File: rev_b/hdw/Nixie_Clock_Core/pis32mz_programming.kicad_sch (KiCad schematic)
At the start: 13 parts, among them J801 PICKIT4, Q801 BSS214NW, SW801 MRST

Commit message: lots of rev B control board schematic progress
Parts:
- renumbered C801 to C?, C802 to C?, D801 to D?, J801 to J?, Q801 to Q?, R805 to R?, R801 to R?, R803 to R?, SW801 to SW?

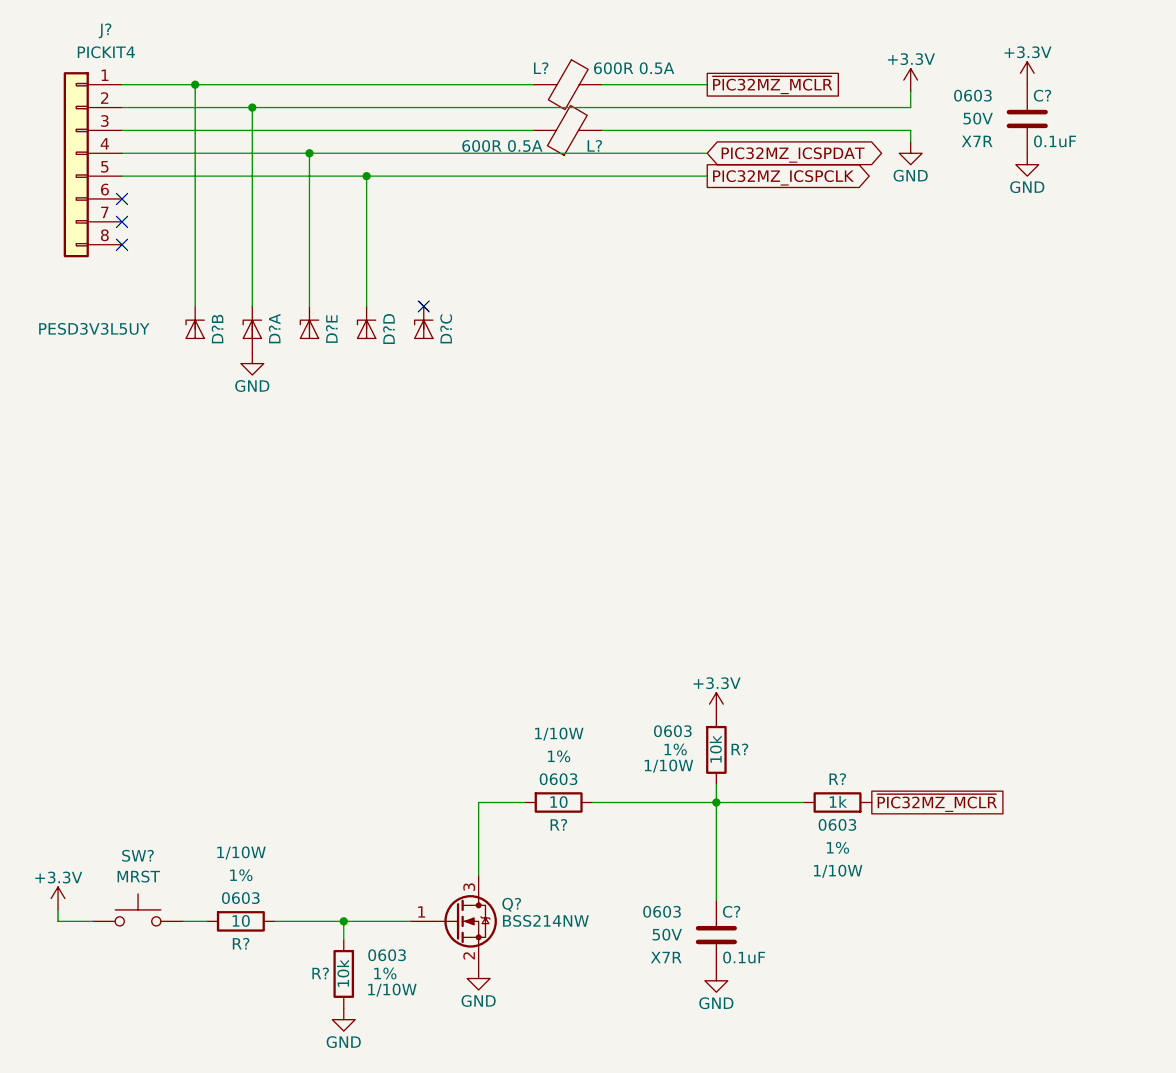
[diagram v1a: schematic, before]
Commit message: updated footprints, ran some DRC
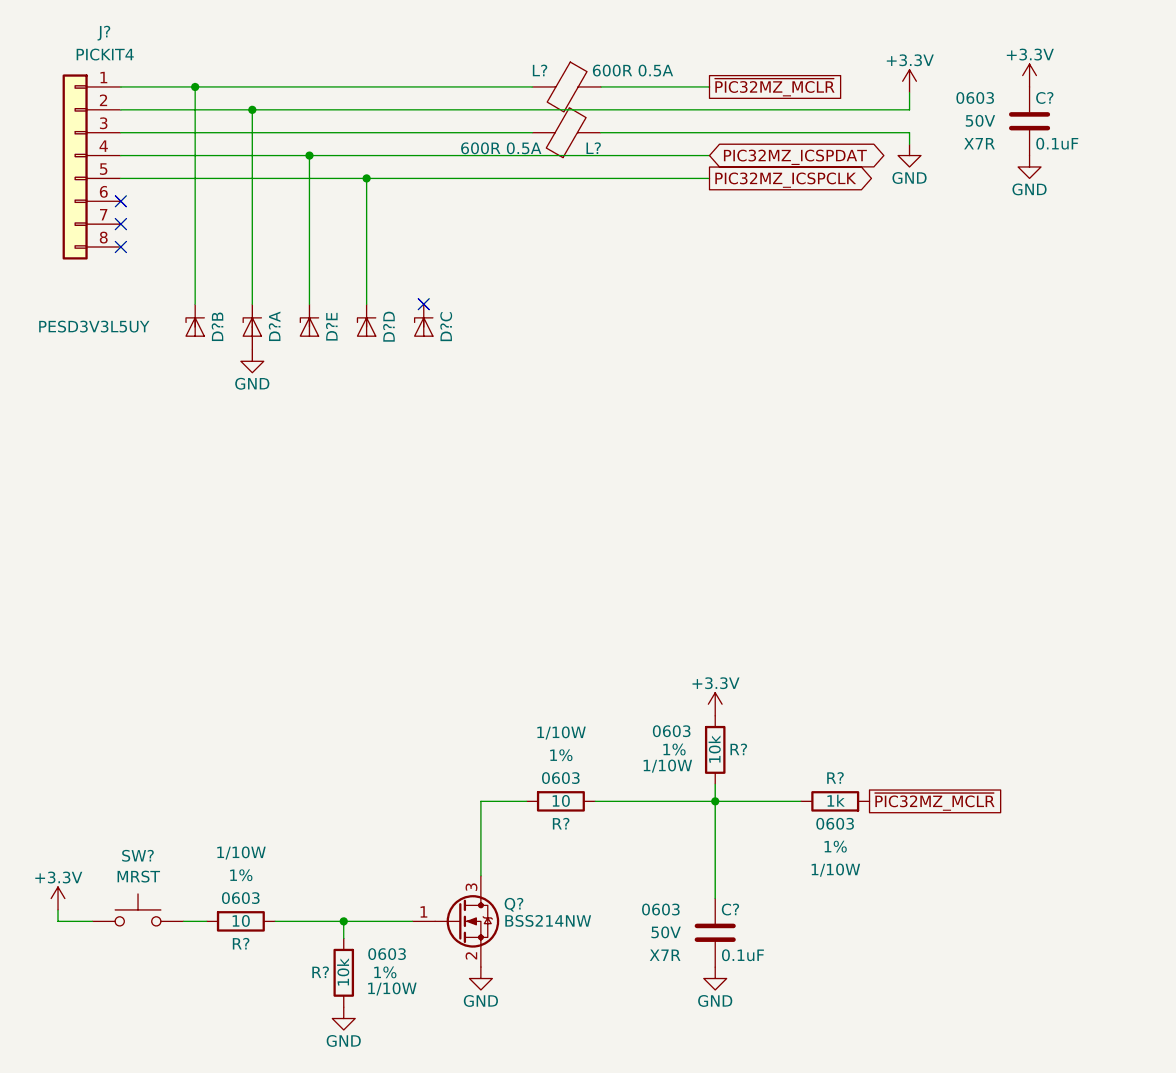
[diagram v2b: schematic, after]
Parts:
- C? (x2): Digi-Key PN 399-7845-1-ND -> (none)
- L? (x2): Digi-Key PN 732-1593-1-ND -> (none)
- R?: Digi-Key PN 311-1.00KHRCT-ND -> (none)
- R? (x4): Digi-Key PN YAG2321CT-ND -> (none)
- SW?: footprint Buttons_Switches_THT:SW_PUSH_6mm -> Button_Switch_THT:SW_PUSH_6mm

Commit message: hid all passive refdes on core PCB
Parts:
- C? (x2): Digi-Key PN (none) -> 1276-1935-1-ND
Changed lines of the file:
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@@
       (effects (font (size 1.27 1.27)) (justify right))
     )
-    (property "Digi-Key PN" "" (at 161.29 130.81 0)
+    (property "Digi-Key PN" "1276-1935-1-ND" (at 161.29 130.81 0)
       (effects (font (size 1.524 1.524)) hide)
     )
@@
       (effects (font (size 1.27 1.27)) (justify right))
     )
-    (property "Digi-Key PN" "" (at 196.215 40.64 0)
+    (property "Digi-Key PN" "1276-1935-1-ND" (at 196.215 40.64 0)
       (effects (font (size 1.524 1.524)) hide)
     )

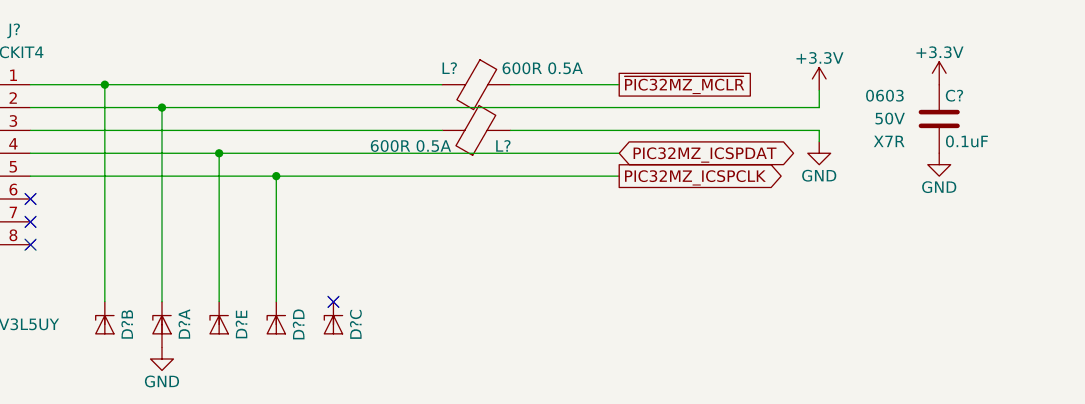
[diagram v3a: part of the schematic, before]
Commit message: added BOM
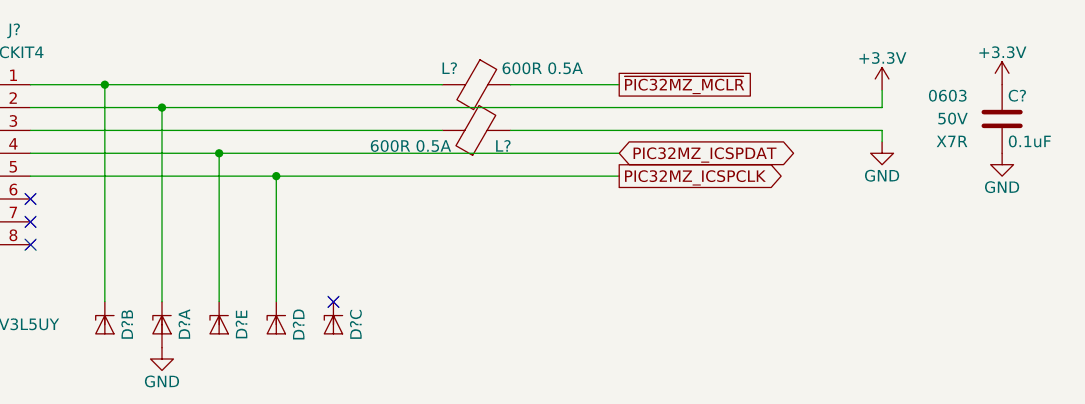
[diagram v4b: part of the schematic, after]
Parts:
- L? (x2): Digi-Key PN (none) -> 490-1014-1-ND
- R?: Digi-Key PN (none) -> 541-1.00KHCT-ND
- R? (x2): Digi-Key PN (none) -> 541-10.0HCT-ND
- R? (x2): Digi-Key PN (none) -> 541-10.0KHCT-ND
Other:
- title: (none) -> Nixie Clock Redux Core Board
- moved on the sheet: C?
